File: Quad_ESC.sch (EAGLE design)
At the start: 28 parts, among them Y1 ECS-80-S-4X

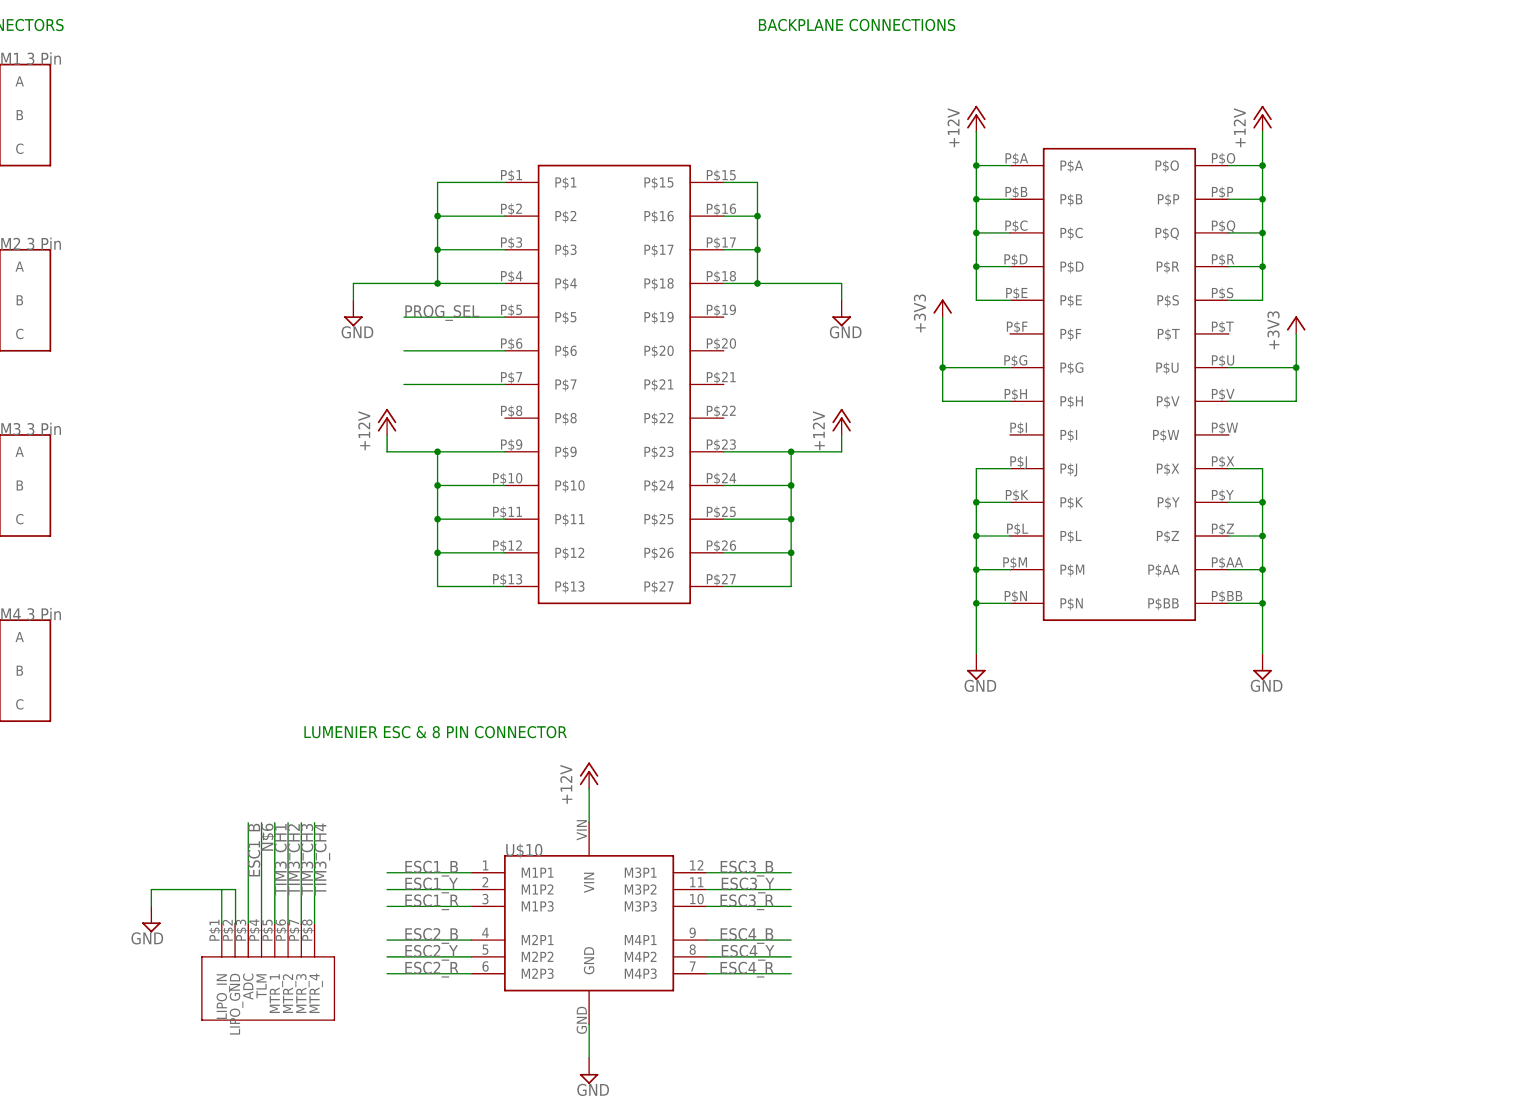
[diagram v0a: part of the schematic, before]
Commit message: Board/Schem Update
added CLT low profile samtec connectors to schem/board, looking at the connector spacing on the board stresses me out ;-;
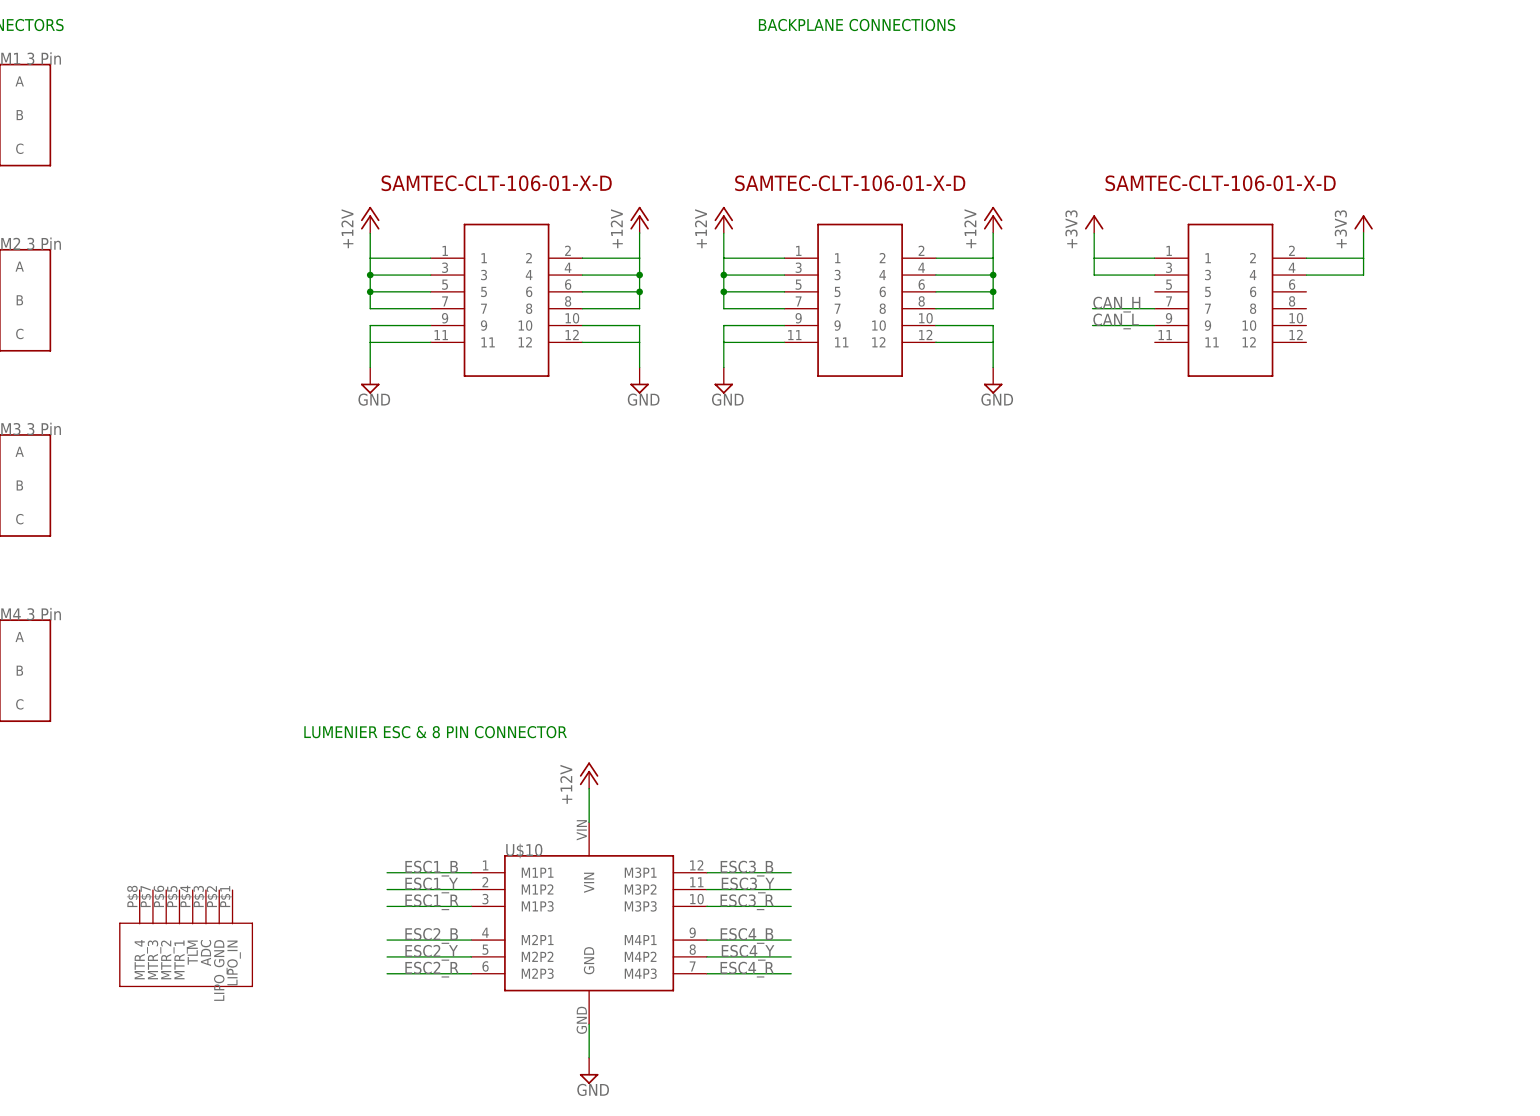
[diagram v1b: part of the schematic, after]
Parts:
- removed U$9: 8PIN_CONNECTOR, BLHeli_32 45A:8PIN_CONNECTOR
- added J1, J2, J3: SAMTEC-CLT-106-01-X-DJ, BLHeli_32 45A:SAMTEC-CLT-106-01-X-DJ
- U$2: value ESC2BACKPLANE -> 8PIN_CONNECTOR; device ESC_to_Backplane_Connectors:ESC2BACKPLANE -> BLHeli_32 45A:8PIN_CONNECTOR
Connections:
- removed net N$10: U$2G$1.P$7
- removed net N$6: U$9.TLM
- removed net N$9: U$2G$1.P$6
- removed net PROG_SEL: U$2G$1.P$5
- net +12V: now also J1.1, J1.2, J1.3, J1.4, J1.5, J1.6, J1.7, J1.8, J2.1, J2.2, J2.3, J2.4, J2.5, J2.6, J2.7, J2.8; no longer U$2G$1.P$10, U$2G$1.P$11, U$2G$1.P$12, U$2G$1.P$13, U$2G$1.P$23, U$2G$1.P$24, U$2G$1.P$25, U$2G$1.P$26, U$2G$1.P$27, U$2G$1.P$9, U$2G$2.P$A, U$2G$2.P$B, U$2G$2.P$C, U$2G$2.P$D, U$2G$2.P$E, U$2G$2.P$O, U$2G$2.P$P, U$2G$2.P$Q, U$2G$2.P$R, U$2G$2.P$S
- net +3V3: now also J3.1, J3.2, J3.3, J3.4; no longer U$2G$2.P$G, U$2G$2.P$H, U$2G$2.P$U, U$2G$2.P$V
- net CAN_H: now also J3.7
- net CAN_L: now also J3.9
- net ESC1_B: no longer U$9.ADC
- net GND: now also J1.10, J1.11, J1.12, J1.9, J2.10, J2.11, J2.12, J2.9; no longer U$2G$1.P$1, U$2G$1.P$15, U$2G$1.P$16, U$2G$1.P$17, U$2G$1.P$18, U$2G$1.P$2, U$2G$1.P$3, U$2G$1.P$4, U$2G$2.P$AA, U$2G$2.P$BB, U$2G$2.P$J, U$2G$2.P$K, U$2G$2.P$L, U$2G$2.P$M, U$2G$2.P$N, U$2G$2.P$X, U$2G$2.P$Y, U$2G$2.P$Z, U$9.LIPO_GND, U$9.LIPO_IN
- net TIM3_CH1: no longer U$9.MTR_1
- net TIM3_CH2: no longer U$9.MTR_2
- net TIM3_CH3: no longer U$9.MTR_3
- net TIM3_CH4: no longer U$9.MTR_4

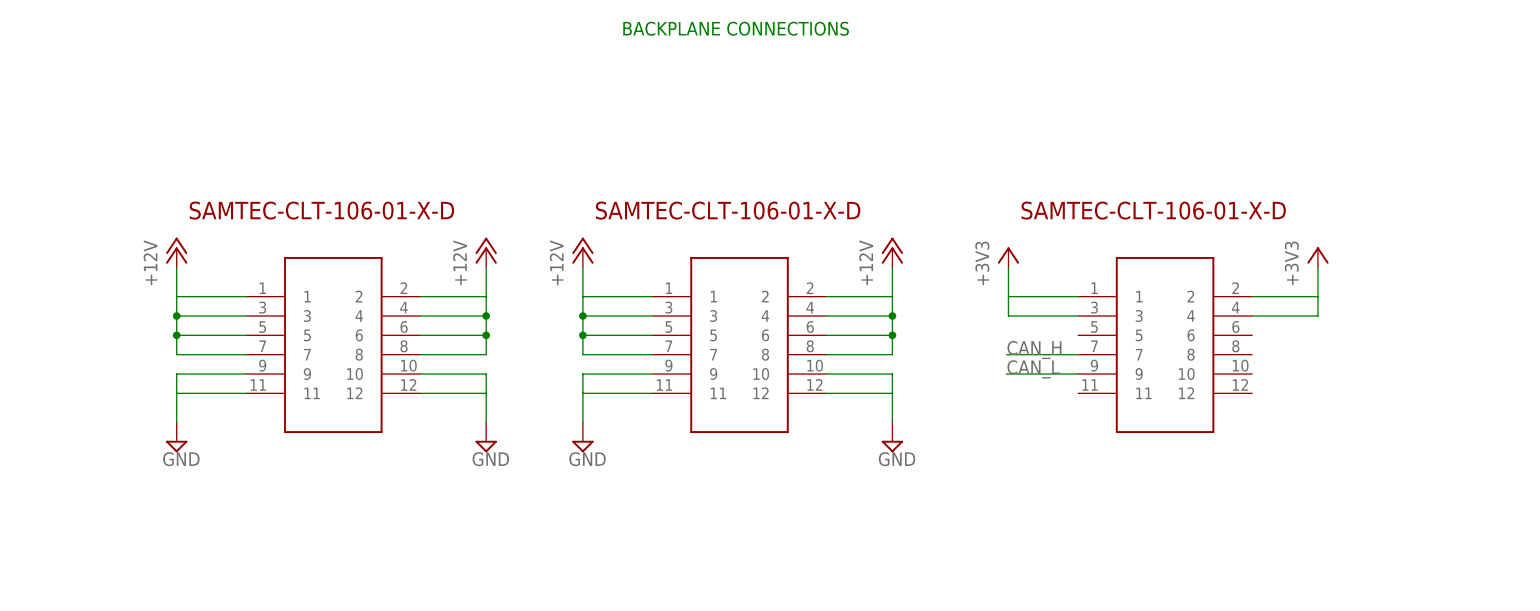
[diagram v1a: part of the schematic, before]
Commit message: Connector Update!!
made new part for backplae connectors with proper spacing, updated schematic and board accordingly
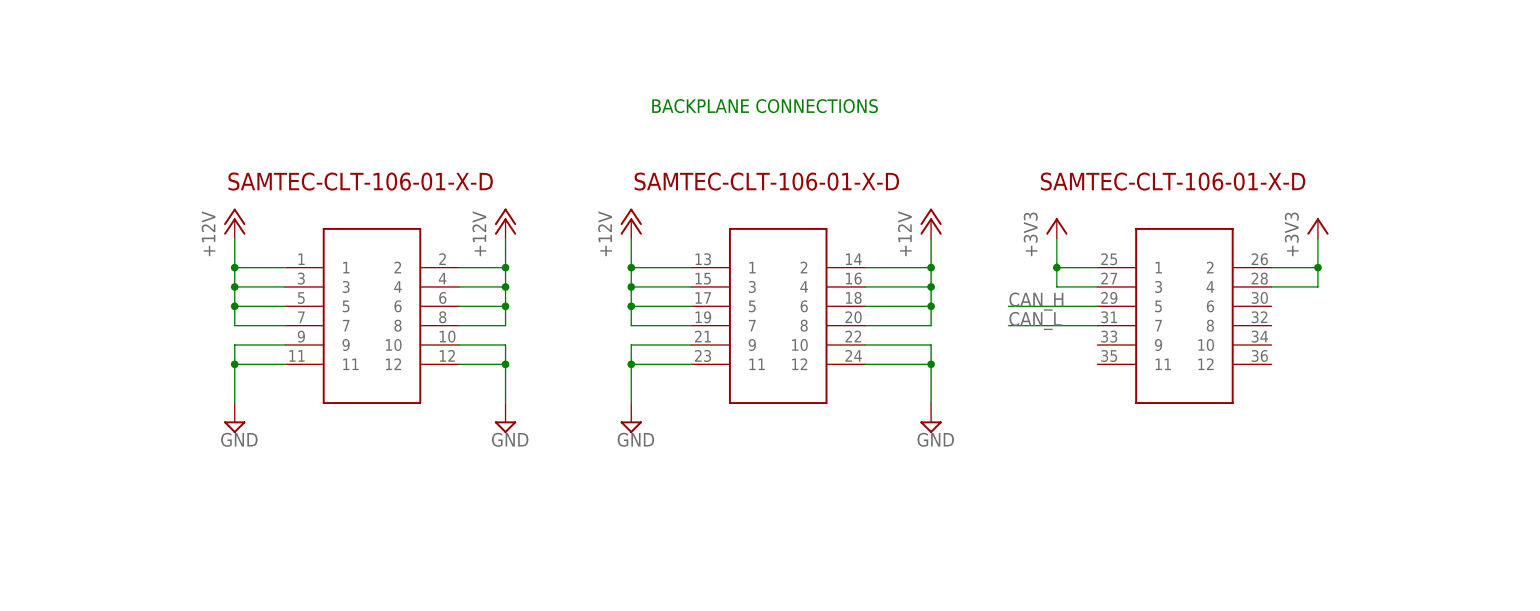
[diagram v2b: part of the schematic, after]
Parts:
- removed J1, J2, J3: SAMTEC-CLT-106-01-X-DJ, BLHeli_32 45A:SAMTEC-CLT-106-01-X-DJ
- added U$3: BACKPLANE_CONNECTORS, BLHeli_32 45A:BACKPLANE_CONNECTORS
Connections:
- net +12V: now also U$3G$1.1, U$3G$1.2, U$3G$1.3, U$3G$1.4, U$3G$1.5, U$3G$1.6, U$3G$1.7, U$3G$1.8, U$3G$2.1, U$3G$2.2, U$3G$2.3, U$3G$2.4, U$3G$2.5, U$3G$2.6, U$3G$2.7, U$3G$2.8; no longer J1.1, J1.2, J1.3, J1.4, J1.5, J1.6, J1.7, J1.8, J2.1, J2.2, J2.3, J2.4, J2.5, J2.6, J2.7, J2.8
- net +3V3: now also U$3G$3.1, U$3G$3.2, U$3G$3.3, U$3G$3.4; no longer J3.1, J3.2, J3.3, J3.4
- net CAN_H: now also U$3G$3.5; no longer J3.7
- net CAN_L: now also U$3G$3.7; no longer J3.9
- net GND: now also U$3G$1.10, U$3G$1.11, U$3G$1.12, U$3G$1.9, U$3G$2.10, U$3G$2.11, U$3G$2.12, U$3G$2.9; no longer J1.10, J1.11, J1.12, J1.9, J2.10, J2.11, J2.12, J2.9

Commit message: Connector Updates, Board Routing
Backplane connectors updated, board routing on right side completed
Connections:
- removed net 3.3V: R4.1
- new net N$3: R4.2, U$4.PA3
- new net N$7: U$3G$3.8
- new net N$8: U$3G$3.12
- new net TLM: U$2.TLM, U$4.PA5
- net +3V3: now also R4.1, U$2.LIPO_IN
- net GND: now also U$2.ADC, U$2.LIPO_GND; no longer R4.2, U$4.PA3
- net NRST: now also U$3G$3.6
- net SWCLK: now also U$3G$3.11
- net SWDIO: now also U$3G$3.9
- net TIM3_CH1: now also U$2.MTR_1
- net TIM3_CH2: now also U$2.MTR_2
- net TIM3_CH3: now also U$2.MTR_3
- net TIM3_CH4: now also U$2.MTR_4
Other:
- note removed: "OSCILLATOR"
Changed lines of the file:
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@@
 <part name="R4" library="SparkFun-Resistors" library_urn="urn:adsk.eagle:library:532" deviceset="10KOHM" device="-0603-1/10W-1%" package3d_urn="urn:adsk.eagle:package:39650/1" value="10k"/>
 <part name="SUPPLY7" library="SparkFun-PowerSymbols" library_urn="urn:adsk.eagle:library:530" deviceset="3.3V" device=""/>
-<part name="SUPPLY8" library="supply2" library_urn="urn:adsk.eagle:library:372" deviceset="GND" device=""/>
 <part name="U$2" library="BLHeli_32 45A" deviceset="8PIN_CONNECTOR" device=""/>
 <part name="U$3" library="BLHeli_32 45A" deviceset="BACKPLANE_CONNECTORS" device=""/>
@@
 <part name="SUPPLY10" library="supply2" library_urn="urn:adsk.eagle:library:372" deviceset="GND" device=""/>
 <part name="SUPPLY11" library="supply2" library_urn="urn:adsk.eagle:library:372" deviceset="GND" device=""/>
+<part name="SUPPLY1" library="supply2" library_urn="urn:adsk.eagle:library:372" deviceset="GND" device=""/>
+<part name="+3V6" library="supply1" library_urn="urn:adsk.eagle:library:371" deviceset="+3V3" device=""/>
 </parts>
 <sheets>
@@
 <text x="331.47" y="150.368" size="1.778" layer="91">PROGRAMMING HEADERS</text>
 <text x="364.49" y="81.28" size="1.778" layer="91">CAN TRANSCEIVER</text>
-<text x="464.82" y="76.2" size="1.778" layer="91">OSCILLATOR</text>
 <text x="83.82" y="66.04" size="1.778" layer="91">LUMENIER ESC &amp; 8 PIN CONNECTOR</text>
 <text x="439.42" y="86.36" size="1.778" layer="91">ID resistor to backplane</text>
@@
 <attribute name="VALUE" x="461.264" y="99.06" size="1.778" layer="96" font="vector" rot="R90" align="top-center"/>
 </instance>
-<instance part="SUPPLY7" gate="G$1" x="452.12" y="93.98" smashed="yes">
-<attribute name="VALUE" x="452.12" y="96.774" size="1.778" layer="96" align="bottom-center"/>
-</instance>
-<instance part="SUPPLY8" gate="GND" x="444.5" y="96.52" smashed="yes">
-<attribute name="VALUE" x="442.595" y="93.345" size="1.778" layer="96"/>
-</instance>
+<instance part="SUPPLY7" gate="G$1" x="452.12" y="93.98" smashed="yes"/>
 <instance part="U$2" gate="G$1" x="76.2" y="38.1" smashed="yes" rot="R180"/>
 <instance part="U$3" gate="G$1" x="119.38" y="135.89" smashed="yes"/>
@@
 <instance part="SUPPLY11" gate="GND" x="101.6" y="121.92" smashed="yes">
 <attribute name="VALUE" x="99.695" y="118.745" size="1.778" layer="96"/>
+</instance>
+<instance part="SUPPLY1" gate="GND" x="78.74" y="52.07" smashed="yes">
+<attribute name="VALUE" x="76.835" y="48.895" size="1.778" layer="96"/>
+</instance>
+<instance part="+3V6" gate="G$1" x="90.17" y="46.99" smashed="yes">
+<attribute name="VALUE" x="87.63" y="41.91" size="1.778" layer="96" rot="R90"/>
 </instance>
 </instances>
@@
 </segment>
 <segment>
-<pinref part="R4" gate="G$1" pin="2"/>
-<pinref part="U$4" gate="G$1" pin="PA3"/>
-<wire x1="459.74" y1="104.14" x2="459.74" y2="106.68" width="0.1524" layer="91"/>
-<wire x1="459.74" y1="106.68" x2="459.74" y2="110.49" width="0.1524" layer="91"/>
-<wire x1="459.74" y1="106.68" x2="444.5" y2="106.68" width="0.1524" layer="91"/>
-<wire x1="444.5" y1="106.68" x2="444.5" y2="99.06" width="0.1524" layer="91"/>
-<junction x="459.74" y="106.68"/>
-<pinref part="SUPPLY8" gate="GND" pin="GND"/>
-</segment>
-<segment>
 <pinref part="U$3" gate="G$2" pin="10"/>
 <wire x1="184.404" y1="132.08" x2="193.04" y2="132.08" width="0.1524" layer="91"/>
@@
 <junction x="101.6" y="129.54"/>
 <pinref part="SUPPLY11" gate="GND" pin="GND"/>
+</segment>
+<segment>
+<pinref part="U$2" gate="G$1" pin="ADC"/>
+<wire x1="69.2" y1="43.1" x2="69.2" y2="57.15" width="0.1524" layer="91"/>
+<wire x1="69.2" y1="57.15" x2="71.2" y2="57.15" width="0.1524" layer="91"/>
+<wire x1="71.2" y1="57.15" x2="78.74" y2="57.15" width="0.1524" layer="91"/>
+<wire x1="78.74" y1="57.15" x2="78.74" y2="54.61" width="0.1524" layer="91"/>
+<pinref part="U$2" gate="G$1" pin="LIPO_GND"/>
+<wire x1="71.2" y1="43.1" x2="71.2" y2="57.15" width="0.1524" layer="91"/>
+<pinref part="SUPPLY1" gate="GND" pin="GND"/>
 </segment>
 </net>
@@
 <junction x="243.84" y="142.24"/>
 <pinref part="+3V9" gate="G$1" pin="+3V3"/>
+</segment>
+<segment>
+<pinref part="U$2" gate="G$1" pin="LIPO_IN"/>
+<wire x1="73.2" y1="43.1" x2="90.17" y2="43.1" width="0.1524" layer="91"/>
+<wire x1="90.17" y1="43.1" x2="90.17" y2="44.45" width="0.1524" layer="91"/>
+<pinref part="+3V6" gate="G$1" pin="+3V3"/>
+</segment>
+<segment>
+<pinref part="R4" gate="G$1" pin="1"/>
+<wire x1="459.74" y1="93.98" x2="459.74" y2="91.44" width="0.1524" layer="91"/>
+<wire x1="459.74" y1="91.44" x2="452.12" y2="91.44" width="0.1524" layer="91"/>
+<wire x1="452.12" y1="91.44" x2="452.12" y2="93.98" width="0.1524" layer="91"/>
+<pinref part="SUPPLY7" gate="G$1" pin="3.3V"/>
+<label x="449.58" y="97.79" size="1.778" layer="95"/>
 </segment>
 </net>
@@
 <label x="467.36" y="96.52" size="1.778" layer="95" rot="R90"/>
 </segment>
+<segment>
+<pinref part="U$2" gate="G$1" pin="MTR_1"/>
+<wire x1="65.2" y1="43.1" x2="65.2" y2="58.34" width="0.1524" layer="91"/>
+<label x="65.2" y="57.07" size="1.778" layer="95" rot="R90" align="bottom-right"/>
+</segment>
 </net>
 <net name="TIM3_CH2" class="0">
@@
 <label x="472.44" y="96.52" size="1.778" layer="95" rot="R90"/>
 </segment>
+<segment>
+<pinref part="U$2" gate="G$1" pin="MTR_2"/>
+<wire x1="63.2" y1="43.1" x2="63.2" y2="58.34" width="0.1524" layer="91"/>
+<label x="63.2" y="57.07" size="1.778" layer="95" rot="R90" align="bottom-right"/>
+</segment>
 </net>
 <net name="TIM3_CH3" class="0">
@@
 <label x="474.98" y="96.52" size="1.778" layer="95" rot="R90"/>
 </segment>
+<segment>
+<pinref part="U$2" gate="G$1" pin="MTR_3"/>
+<wire x1="61.2" y1="43.1" x2="61.2" y2="58.34" width="0.1524" layer="91"/>
+<label x="61.2" y="57.07" size="1.778" layer="95" rot="R90" align="bottom-right"/>
+</segment>
 </net>
 <net name="TIM3_CH4" class="0">
@@
 <label x="477.52" y="96.52" size="1.778" layer="95" rot="R90"/>
 </segment>
+<segment>
+<pinref part="U$2" gate="G$1" pin="MTR_4"/>
+<wire x1="59.2" y1="43.1" x2="59.2" y2="58.34" width="0.1524" layer="91"/>
+<label x="59.2" y="57.07" size="1.778" layer="95" rot="R90" align="bottom-right"/>
+</segment>
 </net>
 <net name="ESC4_B" class="0">
@@
 <label x="350.52" y="134.62" size="1.778" layer="95"/>
 </segment>
+<segment>
+<pinref part="U$3" gate="G$3" pin="9"/>
+<wire x1="214.884" y1="132.08" x2="203.2" y2="132.08" width="0.1524" layer="91"/>
+<label x="203.2" y="132.08" size="1.778" layer="95"/>
+</segment>
 </net>
 <net name="SWCLK" class="0">
@@
 <wire x1="340.36" y1="139.7" x2="355.6" y2="139.7" width="0.1524" layer="91"/>
 <label x="350.52" y="139.7" size="1.778" layer="95"/>
+</segment>
+<segment>
+<pinref part="U$3" gate="G$3" pin="11"/>
+<wire x1="214.884" y1="129.54" x2="203.2" y2="129.54" width="0.1524" layer="91"/>
+<label x="203.2" y="129.54" size="1.778" layer="95"/>
 </segment>
 </net>
@@
 <label x="350.52" y="132.08" size="1.778" layer="95"/>
 </segment>
+<segment>
+<pinref part="U$3" gate="G$3" pin="6"/>
+<wire x1="237.744" y1="137.16" x2="247.65" y2="137.16" width="0.1524" layer="91"/>
+<label x="241.3" y="137.16" size="1.778" layer="95"/>
+</segment>
 </net>
 <net name="OSC_IN" class="0">
@@
 </segment>
 </net>
-<net name="3.3V" class="0">
-<segment>
-<pinref part="R4" gate="G$1" pin="1"/>
-<wire x1="459.74" y1="93.98" x2="459.74" y2="91.44" width="0.1524" layer="91"/>
-<wire x1="459.74" y1="91.44" x2="452.12" y2="91.44" width="0.1524" layer="91"/>
-<wire x1="452.12" y1="91.44" x2="452.12" y2="93.98" width="0.1524" layer="91"/>
-<pinref part="SUPPLY7" gate="G$1" pin="3.3V"/>
-</segment>
-</net>
+<net name="N$3" class="0">
+<segment>
+<pinref part="U$4" gate="G$1" pin="PA3"/>
+<pinref part="R4" gate="G$1" pin="2"/>
+<wire x1="459.74" y1="104.14" x2="459.74" y2="110.49" width="0.1524" layer="91"/>
+</segment>
+</net>
+<net name="TLM" class="0">
+<segment>
+<pinref part="U$2" gate="G$1" pin="TLM"/>
+<wire x1="67.2" y1="43.1" x2="67.2" y2="58.34" width="0.1524" layer="91"/>
+<label x="67.2" y="57.07" size="1.778" layer="95" rot="R90" align="bottom-right"/>
+</segment>
+<segment>
+<pinref part="U$4" gate="G$1" pin="PA5"/>
+<wire x1="464.82" y1="110.49" x2="464.82" y2="101.6" width="0.1524" layer="91"/>
+<label x="464.82" y="102.87" size="1.778" layer="95" rot="R90"/>
+</segment>
+</net>
+<net name="N$7" class="0">
+<segment>
+<pinref part="U$3" gate="G$3" pin="8"/>
+<wire x1="237.744" y1="134.62" x2="247.65" y2="134.62" width="0.1524" layer="91"/>
+</segment>
+</net>
+<net name="N$8" class="0">
+<segment>
+<pinref part="U$3" gate="G$3" pin="12"/>
+<wire x1="237.744" y1="129.54" x2="247.65" y2="129.54" width="0.1524" layer="91"/>
+</segment>
+</net>
